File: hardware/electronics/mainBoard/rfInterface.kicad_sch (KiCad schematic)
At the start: 21 parts, among them J14 CONMHF1-SMD-T, J15 CONMHF1-SMD-T, J16 CONMHF1-SMD-T, J17 CONMHF1-SMD-T, U16 PMA2-162LNA+, U17 QCN-19D+

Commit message: assigned net classes
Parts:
- renumbered C79 to C75, C80 to C76, C81 to C77, C77 to C78, C75 to C79, C78 to C80, C76 to C81, J16 to J14, J17 to J15, J14 to J16, J15 to J17, L5 to L4, L4 to L5, R50 to R53, R51 to R54, R52 to R55
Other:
- note added: "Single ended impedance: 50 Ohms"

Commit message: fixed sch
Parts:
- L4: footprint lib_passives:L_0603 -> lib_passives:L_0402; Current Rating 1A4 -> 1A15; DC Resistance 75mR -> 114mR; DKPN 490-15648-1-ND -> 490-15341-1-ND; MPN LQW18AN15NG8ZD -> LQW15AN15NG8ZD; Resonant Frequency 4600MHz -> 5500MHz
- L5: footprint lib_passives:L_0603 -> lib_passives:L_0402; Current Rating 1A9 -> 1A45; DC Resistance 40mR -> 68mR; DKPN 490-15732-1-ND -> 490-15561-1-ND; MPN LQW18AN6N8C8ZD -> LQW15AN6N8G8ZD; Resonant Frequency 6650MHz -> 7GHz; Tolerance 0.2nH -> 2%
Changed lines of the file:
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@@
 			)
 		)
-		(property "Footprint" "lib_passives:L_0603"
+		(property "Footprint" "lib_passives:L_0402"
 			(at 106.68 80.01 90)
 			(effects
@@
 			)
 		)
-		(property "Datasheet" "datasheets/Murata-Electronics-JELF243A-9133.pdf"
+		(property "Datasheet" "datasheets/Murata-Electronics-JELF243A-9138.pdf"
 			(at 106.68 80.01 90)
 			(effects
@@
 			)
 		)
-		(property "Description" "FIXED IND 6.8NH 1.9A 0.04OHM SMD"
+		(property "Description" "FIXED IND 6.8NH 1.45A 0.068OHM"
 			(at 106.68 81.28 90)
 			(effects
@@
 			)
 		)
-		(property "MPN" "LQW18AN6N8C8ZD"
+		(property "MPN" "LQW15AN6N8G8ZD"
 			(at 106.68 81.28 90)
 			(effects
@@
 			)
 		)
-		(property "DKPN" "490-15732-1-ND"
+		(property "DKPN" "490-15561-1-ND"
 			(at 106.68 81.28 90)
 			(effects
@@
 			)
 		)
-		(property "Tolerance" "0.2nH"
+		(property "Tolerance" "2%"
 			(at 107.95 81.915 0)
 			(do_not_autoplace yes)
@@
 			)
 		)
-		(property "Current Rating" "1A9"
+		(property "Current Rating" "1A45"
 			(at 112.649 81.915 0)
 			(do_not_autoplace yes)
@@
 			)
 		)
-		(property "DC Resistance" "40mR"
+		(property "DC Resistance" "68mR"
 			(at 107.95 83.185 0)
 			(do_not_autoplace yes)
@@
 			)
 		)
-		(property "Resonant Frequency" "6650MHz"
+		(property "Resonant Frequency" "7GHz"
 			(at 112.649 83.185 0)
 			(do_not_autoplace yes)
@@
 			)
 		)
-		(property "Footprint" "lib_passives:L_0603"
+		(property "Footprint" "lib_passives:L_0402"
 			(at 147.32 55.88 90)
 			(effects
@@
 			)
 		)
-		(property "Datasheet" "datasheets/Murata-Electronics-JELF243A-9133.pdf"
+		(property "Datasheet" "datasheets/Murata-Electronics-JELF243A-9138.pdf"
 			(at 147.32 55.88 90)
 			(effects
@@
 			)
 		)
-		(property "Description" "FIXED IND 15NH 1.4A 0.075OHM SMD"
+		(property "Description" "FIXED IND 15NH 1.15A 0.114OHM SM"
 			(at 147.32 57.15 90)
 			(effects
@@
 			)
 		)
-		(property "MPN" "LQW18AN15NG8ZD"
+		(property "MPN" "LQW15AN15NG8ZD"
 			(at 147.32 57.15 90)
 			(effects
@@
 			)
 		)
-		(property "DKPN" "490-15648-1-ND"
+		(property "DKPN" "490-15341-1-ND"
 			(at 147.32 57.15 90)
 			(effects
@@
 			)
 		)
-		(property "Current Rating" "1A4"
+		(property "Current Rating" "1A15"
 			(at 153.289 57.785 0)
 			(do_not_autoplace yes)
@@
 			)
 		)
-		(property "DC Resistance" "75mR"
+		(property "DC Resistance" "114mR"
 			(at 148.59 59.055 0)
 			(do_not_autoplace yes)
@@
 			)
 		)
-		(property "Resonant Frequency" "4600MHz"
+		(property "Resonant Frequency" "5500MHz"
 			(at 153.289 59.055 0)
 			(do_not_autoplace yes)

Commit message: redefined symbol refs
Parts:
- renumbered R53 to R47, R54 to R48, R55 to R49
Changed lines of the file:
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@@
 		(dnp no)
 		(fields_autoplaced yes)
-		(property "Reference" "#PWR0186"
+		(property "Reference" "#PWR0183"
 			(at 114.3 133.35 0)
 			(effects
@@
 			(project "mainBoard"
 				(path "/be16e32f-2ccf-4272-9ec7-94d5fe7a55e0/9566ea48-a930-4cf1-864c-3e42d00ab717"
-					(reference "#PWR0186")
+					(reference "#PWR0183")
 					(unit 1)
 				)
@@
 		(dnp no)
 		(fields_autoplaced yes)
-		(property "Reference" "R54"
+		(property "Reference" "R48"
 			(at 142.24 60.96 0)
 			(do_not_autoplace yes)
@@
 			(project ""
 				(path "/be16e32f-2ccf-4272-9ec7-94d5fe7a55e0/9566ea48-a930-4cf1-864c-3e42d00ab717"
-					(reference "R54")
+					(reference "R48")
 					(unit 1)
 				)
@@
 		(dnp no)
 		(fields_autoplaced yes)
-		(property "Reference" "#PWR0183"
+		(property "Reference" "#PWR0180"
 			(at 228.6 97.79 0)
 			(effects
@@
 			(project "mainBoard"
 				(path "/be16e32f-2ccf-4272-9ec7-94d5fe7a55e0/9566ea48-a930-4cf1-864c-3e42d00ab717"
-					(reference "#PWR0183")
+					(reference "#PWR0180")
 					(unit 1)
 				)
@@
 		(dnp no)
 		(fields_autoplaced yes)
-		(property "Reference" "#PWR0184"
+		(property "Reference" "#PWR0181"
 			(at 114.3 107.95 0)
 			(effects
@@
 			(project "mainBoard"
 				(path "/be16e32f-2ccf-4272-9ec7-94d5fe7a55e0/9566ea48-a930-4cf1-864c-3e42d00ab717"
-					(reference "#PWR0184")
+					(reference "#PWR0181")
 					(unit 1)
 				)
@@
 		(dnp no)
 		(fields_autoplaced yes)
-		(property "Reference" "#PWR0185"
+		(property "Reference" "#PWR0182"
 			(at 91.44 120.65 0)
 			(effects
@@
 			(project "mainBoard"
 				(path "/be16e32f-2ccf-4272-9ec7-94d5fe7a55e0/9566ea48-a930-4cf1-864c-3e42d00ab717"
-					(reference "#PWR0185")
+					(reference "#PWR0182")
 					(unit 1)
 				)
@@
 		(dnp no)
 		(fields_autoplaced yes)
-		(property "Reference" "#PWR0178"
+		(property "Reference" "#PWR0175"
 			(at 91.44 95.25 0)
 			(effects
@@
 			(project "mainBoard"
 				(path "/be16e32f-2ccf-4272-9ec7-94d5fe7a55e0/9566ea48-a930-4cf1-864c-3e42d00ab717"
-					(reference "#PWR0178")
+					(reference "#PWR0175")
 					(unit 1)
 				)
@@
 		(dnp no)
 		(fields_autoplaced yes)
-		(property "Reference" "R53"
+		(property "Reference" "R47"
 			(at 125.73 53.34 0)
 			(do_not_autoplace yes)
@@
 			(project ""
 				(path "/be16e32f-2ccf-4272-9ec7-94d5fe7a55e0/9566ea48-a930-4cf1-864c-3e42d00ab717"
-					(reference "R53")
+					(reference "R47")
 					(unit 1)
 				)
@@
 		(dnp no)
 		(fields_autoplaced yes)
-		(property "Reference" "#PWR0176"
+		(property "Reference" "#PWR0173"
 			(at 86.36 69.85 0)
 			(effects
@@
 			(project "mainBoard"
 				(path "/be16e32f-2ccf-4272-9ec7-94d5fe7a55e0/9566ea48-a930-4cf1-864c-3e42d00ab717"
-					(reference "#PWR0176")
+					(reference "#PWR0173")
 					(unit 1)
 				)
@@
 		(dnp no)
 		(fields_autoplaced yes)
-		(property "Reference" "#PWR0181"
+		(property "Reference" "#PWR0178"
 			(at 163.83 95.25 0)
 			(effects
@@
 			(project "mainBoard"
 				(path "/be16e32f-2ccf-4272-9ec7-94d5fe7a55e0/9566ea48-a930-4cf1-864c-3e42d00ab717"
-					(reference "#PWR0181")
+					(reference "#PWR0178")
 					(unit 1)
 				)
@@
 		(dnp no)
 		(fields_autoplaced yes)
-		(property "Reference" "R55"
+		(property "Reference" "R49"
 			(at 165.1 88.9 0)
 			(do_not_autoplace yes)
@@
 			(project "mainBoard"
 				(path "/be16e32f-2ccf-4272-9ec7-94d5fe7a55e0/9566ea48-a930-4cf1-864c-3e42d00ab717"
-					(reference "R55")
+					(reference "R49")
 					(unit 1)
 				)
@@
 		(dnp no)
 		(fields_autoplaced yes)
-		(property "Reference" "#PWR0177"
+		(property "Reference" "#PWR0174"
 			(at 228.6 77.47 0)
 			(effects
@@
 			(project "mainBoard"
 				(path "/be16e32f-2ccf-4272-9ec7-94d5fe7a55e0/9566ea48-a930-4cf1-864c-3e42d00ab717"
-					(reference "#PWR0177")
+					(reference "#PWR0174")
 					(unit 1)
 				)
@@
 		(dnp no)
 		(fields_autoplaced yes)
-		(property "Reference" "#PWR0175"
+		(property "Reference" "#PWR0172"
 			(at 170.18 63.5 0)
 			(effects
@@
 			(project "mainBoard"
 				(path "/be16e32f-2ccf-4272-9ec7-94d5fe7a55e0/9566ea48-a930-4cf1-864c-3e42d00ab717"
-					(reference "#PWR0175")
+					(reference "#PWR0172")
 					(unit 1)
 				)
@@
 		(dnp no)
 		(fields_autoplaced yes)
-		(property "Reference" "#PWR0179"
+		(property "Reference" "#PWR0176"
 			(at 124.46 95.25 0)
 			(effects
@@
 			(project "mainBoard"
 				(path "/be16e32f-2ccf-4272-9ec7-94d5fe7a55e0/9566ea48-a930-4cf1-864c-3e42d00ab717"
-					(reference "#PWR0179")
+					(reference "#PWR0176")
 					(unit 1)
 				)
@@
 		(dnp no)
 		(fields_autoplaced yes)
-		(property "Reference" "#PWR0182"
+		(property "Reference" "#PWR0179"
 			(at 190.5 95.25 0)
 			(effects
@@
 			(project "mainBoard"
 				(path "/be16e32f-2ccf-4272-9ec7-94d5fe7a55e0/9566ea48-a930-4cf1-864c-3e42d00ab717"
-					(reference "#PWR0182")
+					(reference "#PWR0179")
 					(unit 1)
 				)
@@
 		(dnp no)
 		(fields_autoplaced yes)
-		(property "Reference" "#PWR0180"
+		(property "Reference" "#PWR0177"
 			(at 129.54 95.25 0)
 			(effects
@@
 			(project "mainBoard"
 				(path "/be16e32f-2ccf-4272-9ec7-94d5fe7a55e0/9566ea48-a930-4cf1-864c-3e42d00ab717"
-					(reference "#PWR0180")
-					(unit 1)
-				)
+					(reference "#PWR0177")
+					(unit 1)
+				)

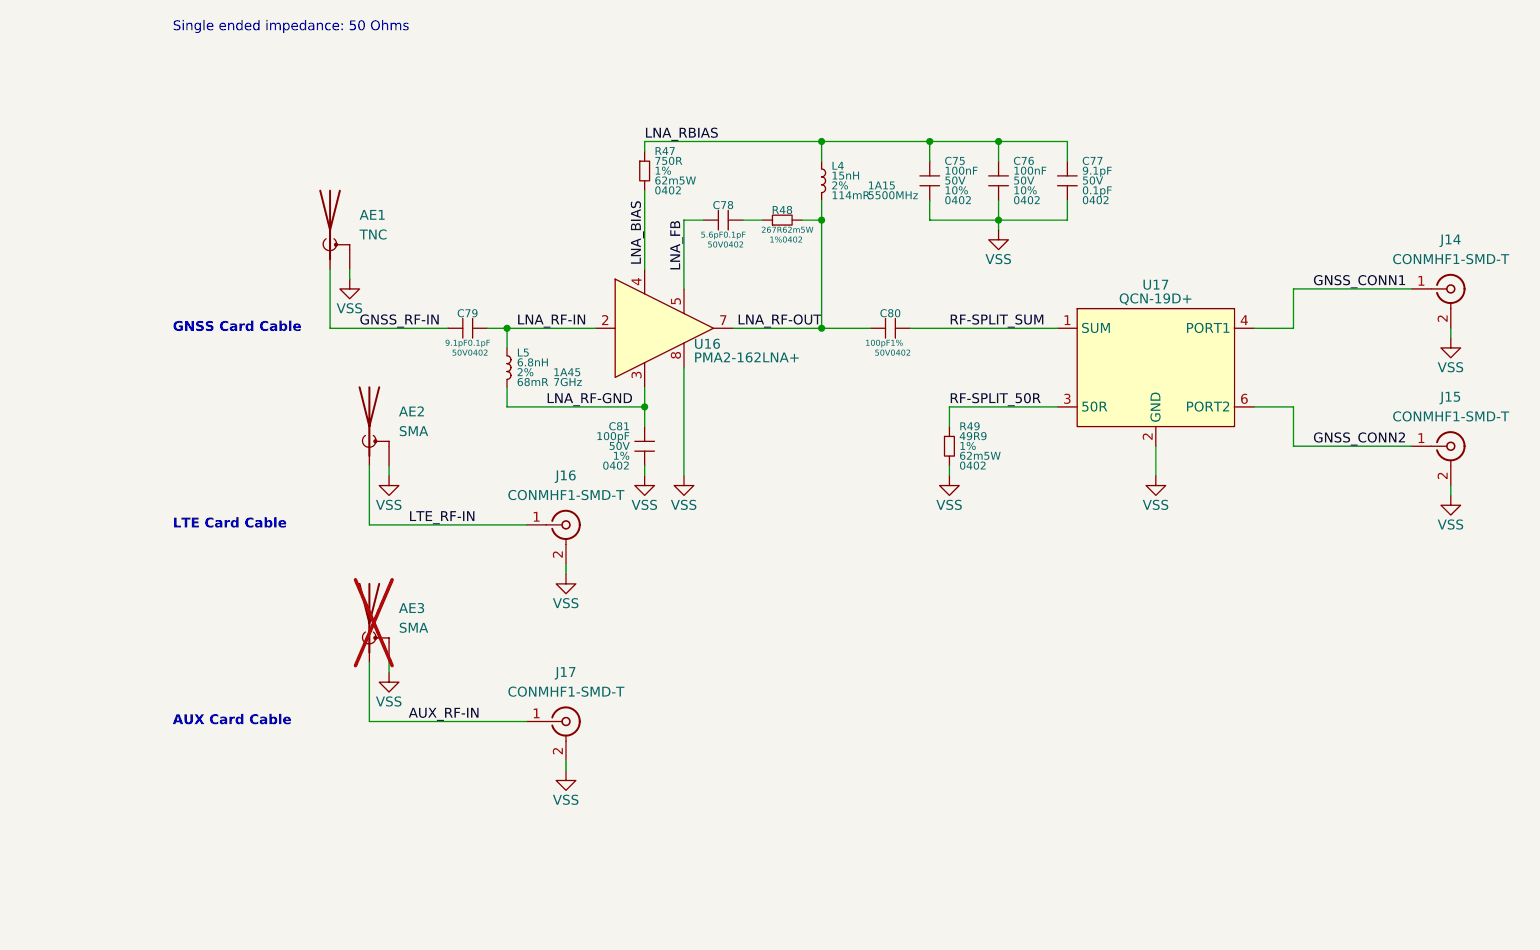
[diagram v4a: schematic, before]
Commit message: fixed net names and added notes
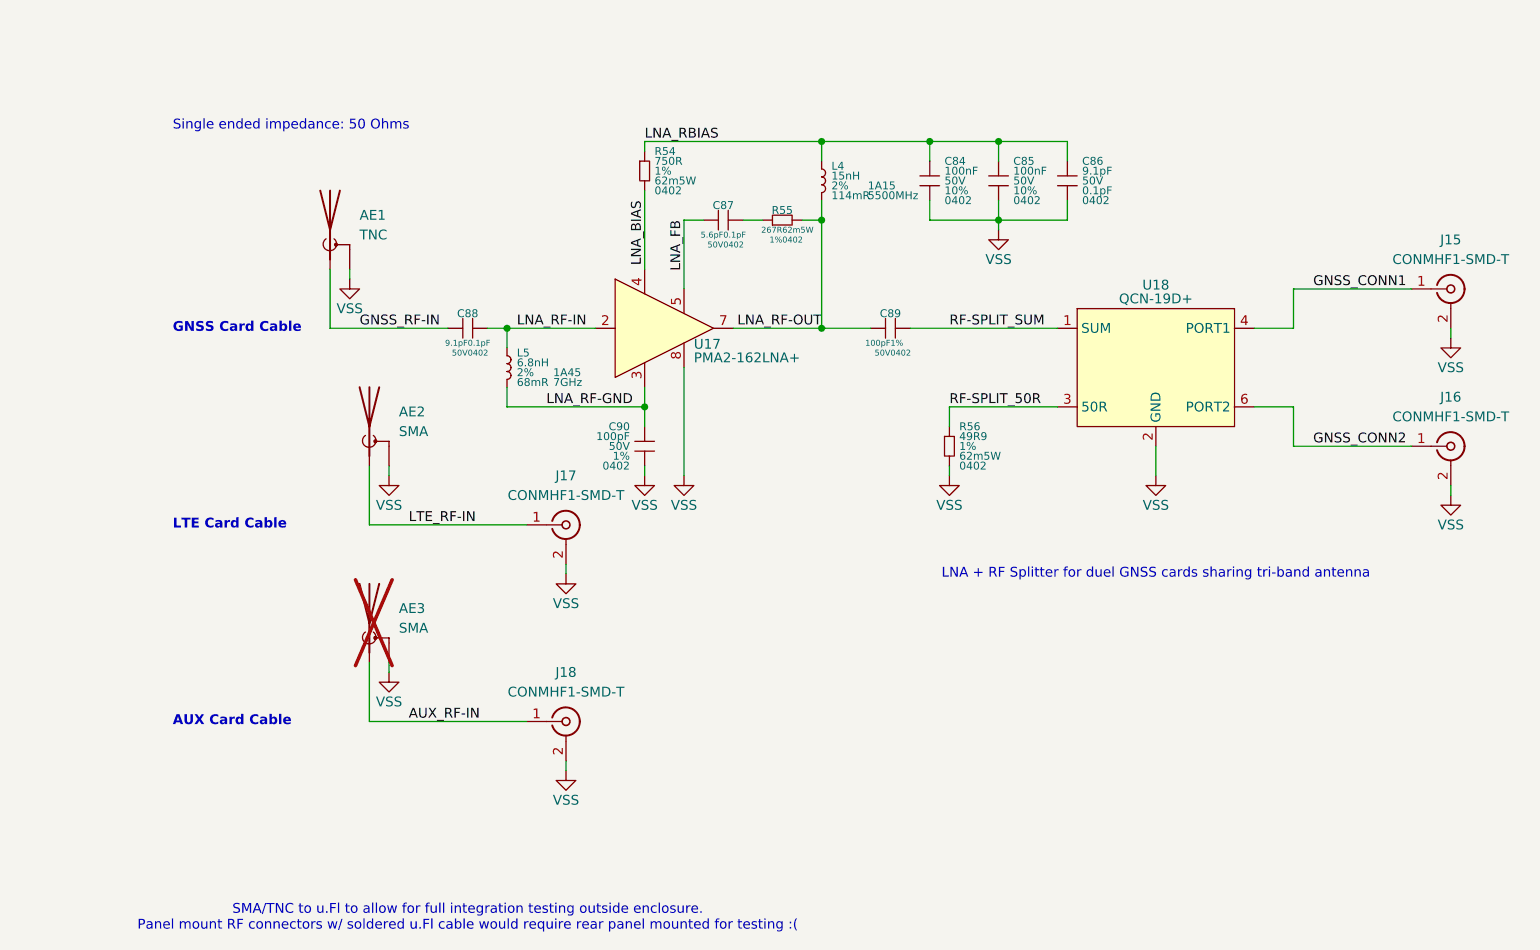
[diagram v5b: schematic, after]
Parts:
- renumbered C75 to C84, C76 to C85, C77 to C86, C78 to C87, C79 to C88, C80 to C89, C81 to C90, J14 to J15, J15 to J16, J16 to J17, J17 to J18, R47 to R54, R48 to R55, R49 to R56, U16 to U17, U17 to U18
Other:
- note added: "LNA + RF Splitter for duel GNSS cards sharing tri-band antenna"
- note added: "SMA/TNC to u.Fl to allow for full integration testing outside enclosure. Panel mount RF connectors w/ soldered u.Fl cable would require rear panel mounted for testing :("
